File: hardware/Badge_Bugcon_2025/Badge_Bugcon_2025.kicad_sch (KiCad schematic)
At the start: 0 parts

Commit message: feat(Hw):Update_Schematic
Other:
- sheet MCU ports: added SCL, SDA; removed none
- sheet OLED ports: added DOWN, LEFT, RIGHT, SCL, SDA, UP, v_3v3; removed none

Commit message: feat(Hw):Update_Schematic
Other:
- sheet MCU ports: added DOWN, LEFT, RIGHT, UP; removed none
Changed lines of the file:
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@@
+	(wire
+		(pts
+			(xy 88.9 114.3) (xy 125.73 114.3)
+		)
+		(stroke
+			(width 0)
+			(type default)
+		)
+	)
 	(wire
 		(pts
@@
 	(wire
 		(pts
+			(xy 88.9 116.84) (xy 125.73 116.84)
+		)
+		(stroke
+			(width 0)
+			(type default)
+		)
+	)
+	(wire
+		(pts
 			(xy 181.61 113.03) (xy 181.61 147.32)
 		)
@@
 	(wire
 		(pts
+			(xy 88.9 111.76) (xy 125.73 111.76)
+		)
+		(stroke
+			(width 0)
+			(type default)
+		)
+	)
+	(wire
+		(pts
 			(xy 62.992 69.85) (xy 62.992 85.09)
 		)
@@
 		(pts
 			(xy 70.612 69.85) (xy 62.992 69.85)
+		)
+		(stroke
+			(width 0)
+			(type default)
+		)
+	)
+	(wire
+		(pts
+			(xy 88.9 109.22) (xy 125.73 109.22)
 		)
 		(stroke
@@
 			(effects
 				(font
+					(size 1.27 1.27)
+				)
+				(justify left)
+			)
+		)
+		(pin "DOWN" bidirectional
+			(at 125.73 114.3 180)
+			(effects
+				(font
+					(size 1.27 1.27)
+				)
+				(justify left)
+			)
+		)
+		(pin "LEFT" bidirectional
+			(at 125.73 111.76 180)
+			(effects
+				(font
+					(size 1.27 1.27)
+				)
+				(justify left)
+			)
+		)
+		(pin "RIGHT" bidirectional
+			(at 125.73 109.22 180)
+			(effects
+				(font
+					(size 1.27 1.27)
+				)
+				(justify left)
+			)
+		)
+		(pin "UP" bidirectional
+			(at 125.73 116.84 180)
+			(effects
+				(font

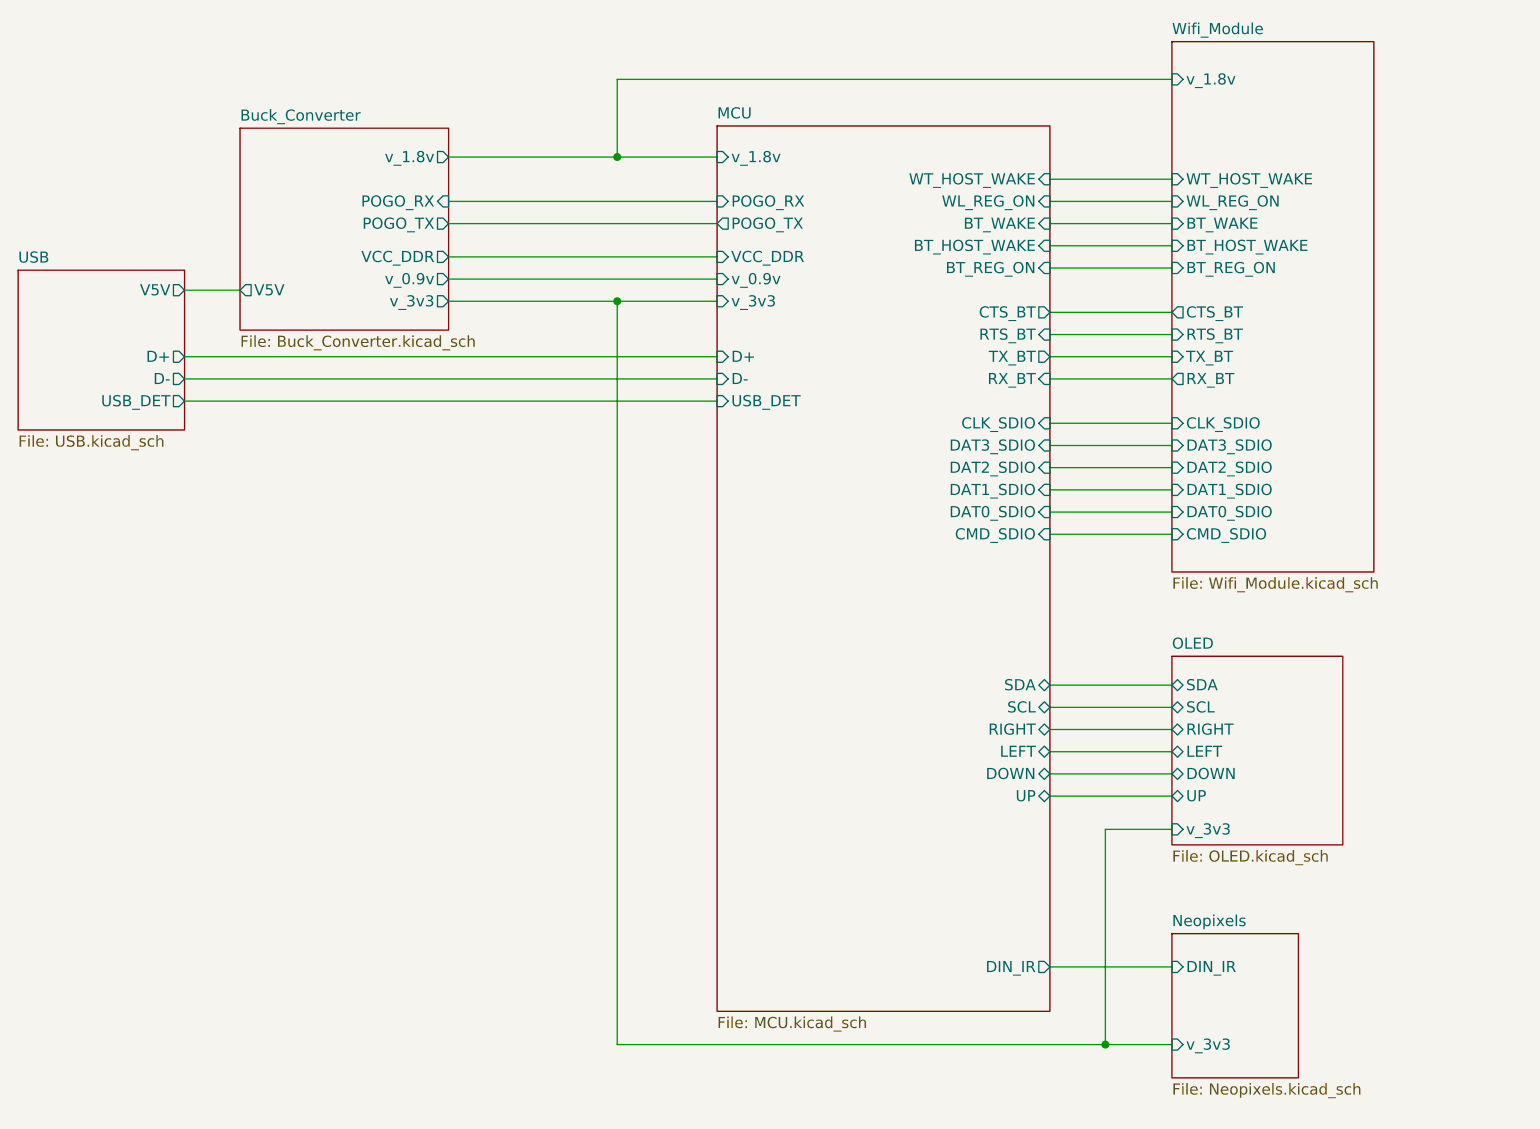
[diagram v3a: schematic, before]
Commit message: feat(Hw):Wifi_Module_Deleted
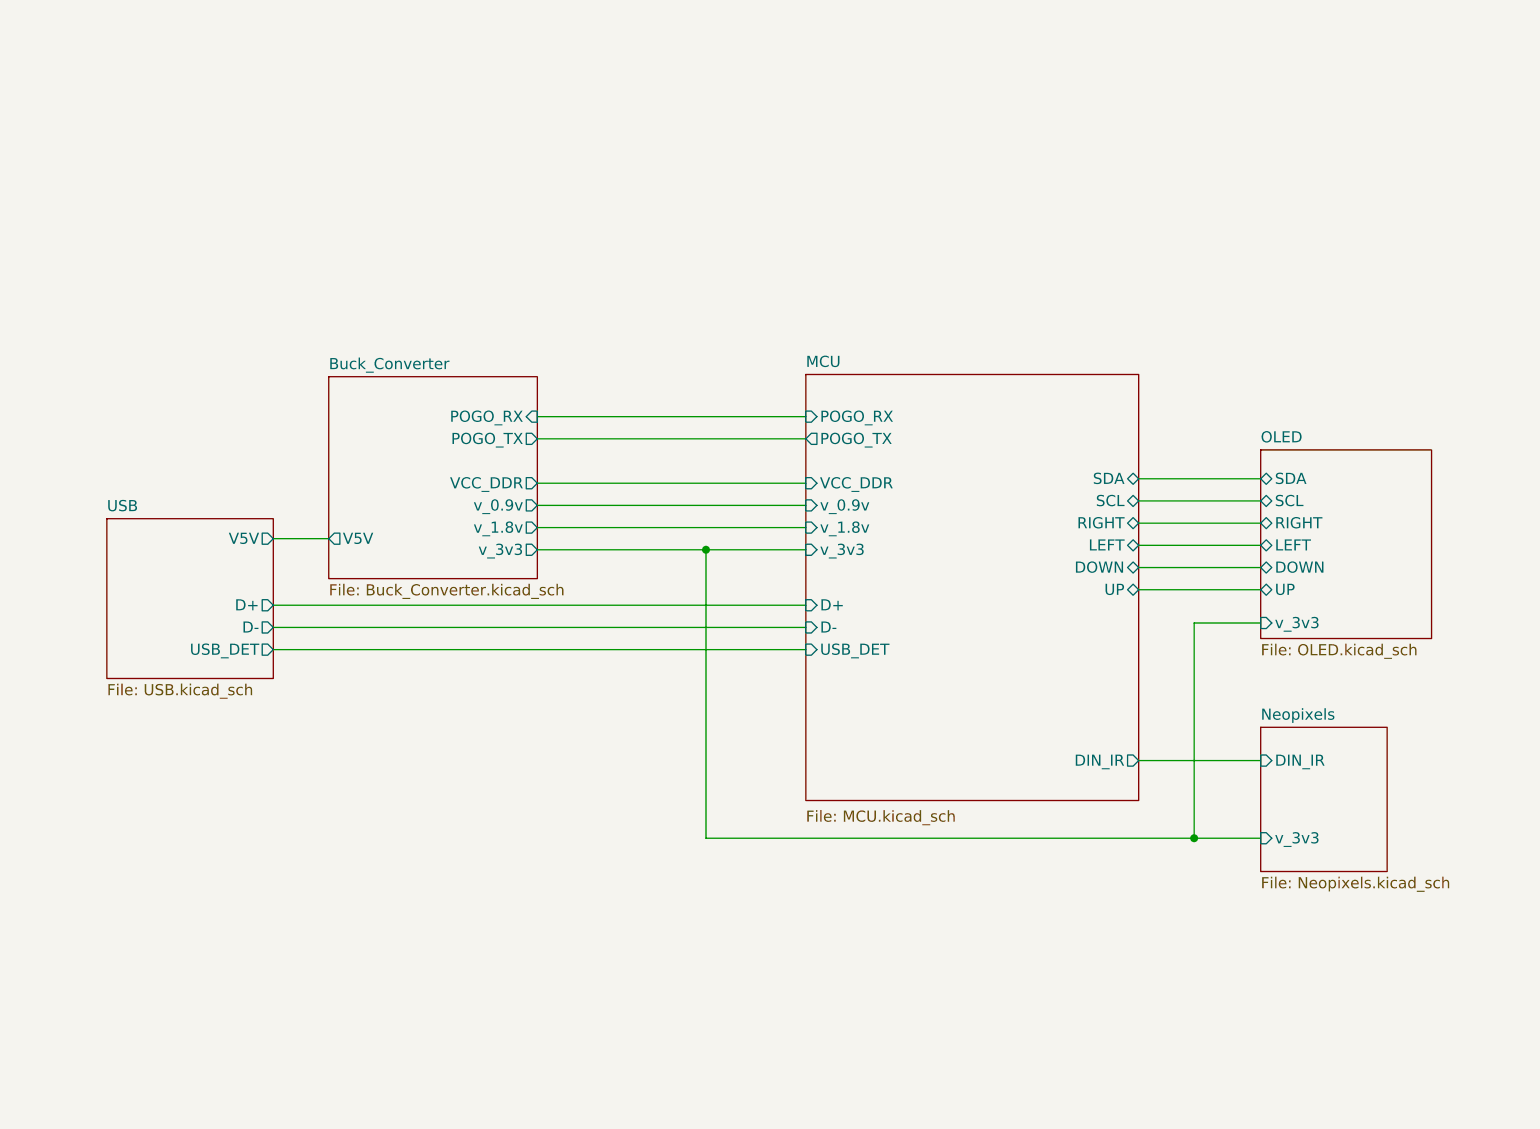
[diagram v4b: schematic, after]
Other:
- removed sheet Wifi_Module
- sheet MCU ports: added none; removed BT_HOST_WAKE, BT_REG_ON, BT_WAKE, CLK_SDIO, CMD_SDIO, CTS_BT, DAT0_SDIO, DAT1_SDIO, DAT2_SDIO, DAT3_SDIO, RTS_BT, RX_BT, TX_BT, WL_REG_ON, WT_HOST_WAKE

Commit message: feat(Hw):Update_Schematic
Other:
- sheet OLED renamed Add-On
- sheet Add-On ports: added none; removed DOWN, LEFT, RIGHT, UP
- sheet MCU ports: added none; removed DOWN, LEFT, RIGHT, UP
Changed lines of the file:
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@@
 	(paper "A4")
 	(junction
-		(at 185.42 116.078)
+		(at 179.07 104.14)
 		(diameter 0)
 		(color 255 23 32 1)
@@
 	(wire
 		(pts
-			(xy 129.54 83.058) (xy 129.54 116.078)
+			(xy 129.54 83.058) (xy 129.54 104.14)
 		)
 		(stroke
@@
 	(wire
 		(pts
-			(xy 179.07 77.47) (xy 193.04 77.47)
+			(xy 172.72 72.39) (xy 186.69 72.39)
 		)
 		(stroke
@@
 	(wire
 		(pts
-			(xy 179.07 82.55) (xy 193.04 82.55)
-		)
-		(stroke
-			(width 0)
-			(type default)
-		)
-	)
-	(wire
-		(pts
-			(xy 185.42 91.44) (xy 185.42 116.078)
+			(xy 179.07 78.74) (xy 179.07 104.14)
 		)
 		(stroke
@@
 	(wire
 		(pts
-			(xy 185.42 91.44) (xy 193.04 91.44)
+			(xy 179.07 78.74) (xy 186.69 78.74)
 		)
 		(stroke
@@
 	(wire
 		(pts
-			(xy 179.07 107.188) (xy 193.04 107.188)
+			(xy 172.72 93.98) (xy 186.69 93.98)
 		)
 		(stroke
@@
 	(wire
 		(pts
-			(xy 179.07 80.01) (xy 193.04 80.01)
-		)
-		(stroke
-			(width 0)
-			(type default)
-		)
-	)
-	(wire
-		(pts
-			(xy 179.07 85.09) (xy 193.04 85.09)
-		)
-		(stroke
-			(width 0)
-			(type default)
-		)
-	)
-	(wire
-		(pts
-			(xy 179.07 87.63) (xy 193.04 87.63)
-		)
-		(stroke
-			(width 0)
-			(type default)
-		)
-	)
-	(wire
-		(pts
 			(xy 80.01 89.408) (xy 140.97 89.408)
 		)
@@
 	(wire
 		(pts
-			(xy 185.42 116.078) (xy 193.04 116.078)
+			(xy 179.07 104.14) (xy 186.69 104.14)
 		)
 		(stroke
@@
 	(wire
 		(pts
-			(xy 179.07 74.93) (xy 193.04 74.93)
-		)
-		(stroke
-			(width 0)
-			(type default)
-		)
-	)
-	(wire
-		(pts
-			(xy 129.54 116.078) (xy 185.42 116.078)
+			(xy 172.72 69.85) (xy 186.69 69.85)
+		)
+		(stroke
+			(width 0)
+			(type default)
+		)
+	)
+	(wire
+		(pts
+			(xy 129.54 104.14) (xy 179.07 104.14)
 		)
 		(stroke
@@
 	)
 	(sheet
-		(at 193.04 71.628)
-		(size 19.558 21.59)
+		(at 186.69 65.024)
+		(size 19.558 16.764)
 		(exclude_from_sim no)
 		(in_bom yes)
@@
 			(color 0 0 0 0.0000)
 		)
-		(property "Sheetname" "OLED"
-			(at 193.04 70.9164 0)
+		(property "Sheetname" "Add-On"
+			(at 186.69 64.3124 0)
 			(effects
 				(font
@@
 		)
 		(property "Sheetfile" "OLED.kicad_sch"
-			(at 193.04 93.8026 0)
+			(at 186.69 82.3726 0)
 			(effects
 				(font
@@
 			)
 		)
-		(pin "DOWN" bidirectional
-			(at 193.04 85.09 180)
-			(effects
-				(font
-					(size 1.27 1.27)
-				)
-				(justify left)
-			)
-		)
-		(pin "LEFT" bidirectional
-			(at 193.04 82.55 180)
-			(effects
-				(font
-					(size 1.27 1.27)
-				)
-				(justify left)
-			)
-		)
-		(pin "RIGHT" bidirectional
-			(at 193.04 80.01 180)
-			(effects
-				(font
-					(size 1.27 1.27)
-				)
-				(justify left)
-			)
-		)
 		(pin "SCL" bidirectional
-			(at 193.04 77.47 180)
+			(at 186.69 72.39 180)
 			(effects
 				(font
@@
 		)
 		(pin "SDA" bidirectional
-			(at 193.04 74.93 180)
-			(effects
-				(font
-					(size 1.27 1.27)
-				)
-				(justify left)
-			)
-		)
-		(pin "UP" bidirectional
-			(at 193.04 87.63 180)
+			(at 186.69 69.85 180)
 			(effects
 				(font
@@
 		)
 		(pin "v_3v3" input
-			(at 193.04 91.44 180)
+			(at 186.69 78.74 180)
 			(effects
 				(font
@@
 	)
 	(sheet
-		(at 193.04 103.378)
-		(size 14.478 16.51)
+		(at 186.69 90.17)
+		(size 14.478 17.78)
 		(exclude_from_sim no)
 		(in_bom yes)
@@
 		)
 		(property "Sheetname" "Neopixels"
-			(at 193.04 102.6664 0)
+			(at 186.69 89.4584 0)
 			(effects
 				(font
@@
 		)
 		(property "Sheetfile" "Neopixels.kicad_sch"
-			(at 193.04 120.4726 0)
+			(at 186.69 108.5346 0)
 			(effects
 				(font
@@
 		)
 		(pin "DIN_IR" input
-			(at 193.04 107.188 180)
+			(at 186.69 93.98 180)
 			(effects
 				(font
@@
 		)
 		(pin "v_3v3" input
-			(at 193.04 116.078 180)
+			(at 186.69 104.14 180)
 			(effects
 				(font
@@
 	(sheet
 		(at 140.97 62.992)
-		(size 38.1 48.768)
+		(size 31.75 36.83)
 		(exclude_from_sim no)
 		(in_bom yes)
@@
 		)
 		(property "Sheetfile" "MCU.kicad_sch"
-			(at 140.97 112.8526 0)
+			(at 140.97 100.33 0)
 			(effects
 				(font
@@
 		)
 		(pin "DIN_IR" output
-			(at 179.07 107.188 0)
-			(effects
-				(font
-					(size 1.27 1.27)
-				)
-				(justify right)
-			)
-		)
-		(pin "DOWN" bidirectional
-			(at 179.07 85.09 0)
-			(effects
-				(font
-					(size 1.27 1.27)
-				)
-				(justify right)
-			)
-		)
-		(pin "LEFT" bidirectional
-			(at 179.07 82.55 0)
-			(effects
-				(font
-					(size 1.27 1.27)
-				)
-				(justify right)
-			)
-		)
-		(pin "RIGHT" bidirectional
-			(at 179.07 80.01 0)
+			(at 172.72 93.98 0)
 			(effects
 				(font
@@
 		)
 		(pin "SCL" bidirectional
-			(at 179.07 77.47 0)
+			(at 172.72 72.39 0)
 			(effects
 				(font
@@
 		)
 		(pin "SDA" bidirectional
-			(at 179.07 74.93 0)
-			(effects
-				(font
-					(size 1.27 1.27)
-				)
-				(justify right)
-			)
-		)
-		(pin "UP" bidirectional
-			(at 179.07 87.63 0)
-			(effects
-				(font
+			(at 172.72 69.85 0)
+			(effects
+				(font

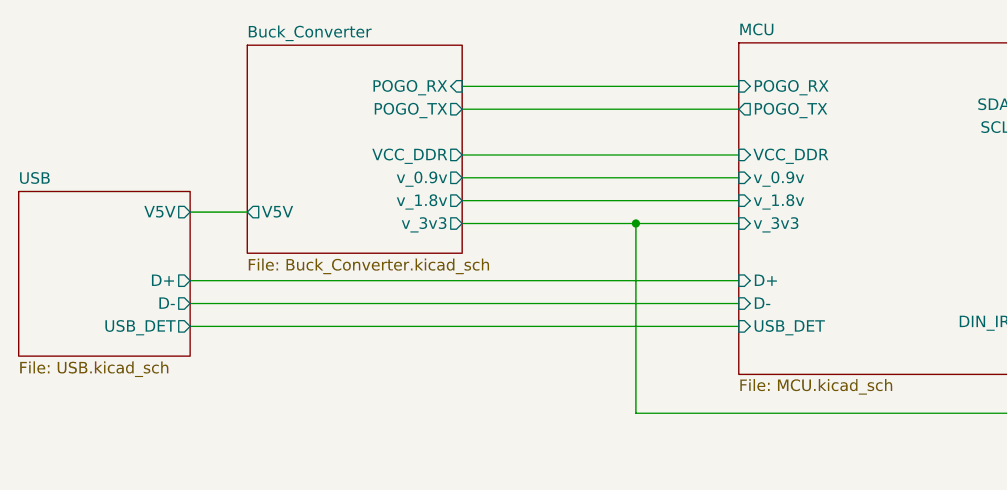
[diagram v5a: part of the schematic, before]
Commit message: feat(Hw):Update_Schematic_And_Floorplan
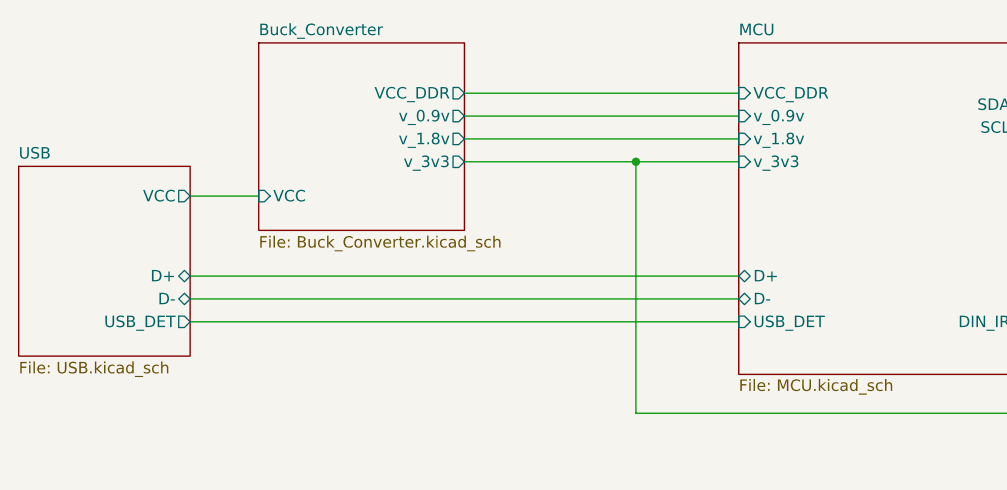
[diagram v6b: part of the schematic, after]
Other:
- sheet Buck_Converter ports: added VCC; removed POGO_RX, POGO_TX, V5V
- sheet MCU ports: added none; removed POGO_RX, POGO_TX
- sheet USB ports: added VCC; removed V5V
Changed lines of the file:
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@@
 	)
 	(junction
-		(at 129.54 83.058)
+		(at 129.54 76.2)
 		(diameter 0)
 		(color 255 23 32 1)
@@
 	(wire
 		(pts
-			(xy 110.236 83.058) (xy 129.54 83.058)
-		)
-		(stroke
-			(width 0)
-			(type default)
-			(color 255 23 32 1)
-		)
-	)
-	(wire
-		(pts
-			(xy 129.54 83.058) (xy 129.54 104.14)
+			(xy 80.01 80.01) (xy 87.63 80.01)
+		)
+		(stroke
+			(width 0)
+			(type default)
+		)
+	)
+	(wire
+		(pts
+			(xy 110.49 76.2) (xy 129.54 76.2)
+		)
+		(stroke
+			(width 0)
+			(type default)
+			(color 255 23 32 1)
+		)
+	)
+	(wire
+		(pts
+			(xy 129.54 76.2) (xy 129.54 104.14)
 		)
 		(stroke
@@
 	(wire
 		(pts
-			(xy 80.01 94.488) (xy 140.97 94.488)
-		)
-		(stroke
-			(width 0)
-			(type default)
-		)
-	)
-	(wire
-		(pts
-			(xy 110.236 80.518) (xy 140.97 80.518)
+			(xy 80.01 93.98) (xy 140.97 93.98)
+		)
+		(stroke
+			(width 0)
+			(type default)
+		)
+	)
+	(wire
+		(pts
+			(xy 110.49 73.66) (xy 140.97 73.66)
 		)
 		(stroke
@@
 	(wire
 		(pts
-			(xy 80.01 81.788) (xy 86.36 81.788)
-		)
-		(stroke
-			(width 0)
-			(type default)
-		)
-	)
-	(wire
-		(pts
 			(xy 172.72 93.98) (xy 186.69 93.98)
 		)
@@
 	(wire
 		(pts
-			(xy 110.236 77.978) (xy 140.97 77.978)
-		)
-		(stroke
-			(width 0)
-			(type default)
-		)
-	)
-	(wire
-		(pts
-			(xy 80.01 91.948) (xy 140.97 91.948)
-		)
-		(stroke
-			(width 0)
-			(type default)
-		)
-	)
-	(wire
-		(pts
-			(xy 129.54 83.058) (xy 140.97 83.058)
-		)
-		(stroke
-			(width 0)
-			(type default)
-			(color 255 23 32 1)
-		)
-	)
-	(wire
-		(pts
-			(xy 80.01 89.408) (xy 140.97 89.408)
-		)
-		(stroke
-			(width 0)
-			(type default)
+			(xy 110.49 71.12) (xy 140.97 71.12)
+		)
+		(stroke
+			(width 0)
+			(type default)
+		)
+	)
+	(wire
+		(pts
+			(xy 129.54 76.2) (xy 140.97 76.2)
+		)
+		(stroke
+			(width 0)
+			(type default)
+			(color 255 23 32 1)
 		)
 	)
@@
 	(wire
 		(pts
-			(xy 110.236 75.438) (xy 140.97 75.438)
+			(xy 110.49 68.58) (xy 140.97 68.58)
 		)
 		(stroke
@@
 	(wire
 		(pts
-			(xy 110.236 70.358) (xy 140.97 70.358)
-		)
-		(stroke
-			(width 0)
-			(type default)
-		)
-	)
-	(wire
-		(pts
-			(xy 110.236 67.818) (xy 140.97 67.818)
+			(xy 80.01 91.44) (xy 140.97 91.44)
+		)
+		(stroke
+			(width 0)
+			(type default)
+		)
+	)
+	(wire
+		(pts
+			(xy 80.01 88.9) (xy 140.97 88.9)
 		)
 		(stroke
@@
 	)
 	(sheet
-		(at 86.36 63.246)
-		(size 23.876 23.114)
+		(at 87.63 62.992)
+		(size 22.86 20.828)
 		(exclude_from_sim no)
 		(in_bom yes)
@@
 		)
 		(property "Sheetname" "Buck_Converter"
-			(at 86.36 62.5344 0)
+			(at 87.63 62.2804 0)
 			(effects
 				(font
@@
 		)
 		(property "Sheetfile" "Buck_Converter.kicad_sch"
-			(at 86.36 86.9446 0)
+			(at 87.63 84.4046 0)
 			(effects
 				(font
@@
 			)
 		)
-		(pin "POGO_RX" input
-			(at 110.236 67.818 0)
-			(effects
-				(font
-					(size 1.27 1.27)
-				)
-				(justify right)
-			)
-		)
-		(pin "POGO_TX" output
-			(at 110.236 70.358 0)
-			(effects
-				(font
-					(size 1.27 1.27)
-				)
-				(justify right)
-			)
-		)
-		(pin "V5V" output
-			(at 86.36 81.788 180)
-			(effects
-				(font
-					(size 1.27 1.27)
-				)
-				(justify left)
-			)
-		)
 		(pin "VCC_DDR" output
-			(at 110.236 75.438 0)
+			(at 110.49 68.58 0)
 			(effects
 				(font
@@
 		)
 		(pin "v_0.9v" output
-			(at 110.236 77.978 0)
+			(at 110.49 71.12 0)
 			(effects
 				(font
@@
 		)
 		(pin "v_1.8v" output
-			(at 110.236 80.518 0)
+			(at 110.49 73.66 0)
 			(effects
 				(font
@@
 		)
 		(pin "v_3v3" output
-			(at 110.236 83.058 0)
-			(effects
-				(font
-					(size 1.27 1.27)
-				)
-				(justify right)
+			(at 110.49 76.2 0)
+			(effects
+				(font
+					(size 1.27 1.27)
+				)
+				(justify right)
+			)
+		)
+		(pin "VCC" input
+			(at 87.63 80.01 180)
+			(effects
+				(font
+					(size 1.27 1.27)
+				)
+				(justify left)
 			)
 		)
@@
 	)
 	(sheet
-		(at 60.96 79.502)
-		(size 19.05 18.288)
+		(at 60.96 76.708)
+		(size 19.05 21.082)
 		(exclude_from_sim no)
 		(in_bom yes)
@@
 		)
 		(property "Sheetname" "USB"
-			(at 60.96 78.7904 0)
+			(at 60.96 75.9964 0)
 			(effects
 				(font
@@
 			)
 		)
-		(pin "D+" output
-			(at 80.01 89.408 0)
-			(effects
-				(font
-					(size 1.27 1.27)
-				)
-				(justify right)
-			)
-		)
-		(pin "D-" output
-			(at 80.01 91.948 0)
-			(effects
-				(font
-					(size 1.27 1.27)
-				)
-				(justify right)
-			)
-		)
 		(pin "USB_DET" output
-			(at 80.01 94.488 0)
-			(effects
-				(font
-					(size 1.27 1.27)
-				)
-				(justify right)
-			)
-		)
-		(pin "V5V" output
-			(at 80.01 81.788 0)
+			(at 80.01 93.98 0)
+			(effects
+				(font
+					(size 1.27 1.27)
+				)
+				(justify right)
+			)
+		)
+		(pin "VCC" output
+			(at 80.01 80.01 0)
+			(effects
+				(font
+					(size 1.27 1.27)
+				)
+				(justify right)
+			)
+		)
+		(pin "D+" bidirectional
+			(at 80.01 88.9 0)
+			(effects
+				(font
+					(size 1.27 1.27)
+				)
+				(justify right)
+			)
+		)
+		(pin "D-" bidirectional
+			(at 80.01 91.44 0)
 			(effects
 				(font
@@
 			)
 		)
-		(pin "POGO_RX" input
-			(at 140.97 67.818 180)
-			(effects
-				(font
-					(size 1.27 1.27)
-				)
-				(justify left)
-			)
-		)
-		(pin "POGO_TX" output
-			(at 140.97 70.358 180)
-			(effects
-				(font
-					(size 1.27 1.27)
-				)
-				(justify left)
-			)
-		)
 		(pin "VCC_DDR" input
-			(at 140.97 75.438 180)
+			(at 140.97 68.58 180)
 			(effects
 				(font
@@
 		)
 		(pin "v_0.9v" input
-			(at 140.97 77.978 180)
+			(at 140.97 71.12 180)
 			(effects
 				(font
@@
 		)
 		(pin "v_1.8v" input
-			(at 140.97 80.518 180)
+			(at 140.97 73.66 180)
 			(effects
 				(font
@@
 		)
 		(pin "v_3v3" input
-			(at 140.97 83.058 180)
-			(effects
-				(font
-					(size 1.27 1.27)
-				)
-				(justify left)
-			)
-		)
-		(pin "D+" input
-			(at 140.97 89.408 180)
-			(effects
-				(font
-					(size 1.27 1.27)
-				)
-				(justify left)
-			)
-		)
-		(pin "D-" input
-			(at 140.97 91.948 180)
+			(at 140.97 76.2 180)
 			(effects
 				(font
@@
 		)
 		(pin "USB_DET" input
-			(at 140.97 94.488 180)
+			(at 140.97 93.98 180)
 			(effects
 				(font
@@
 			)
 		)
+		(pin "D+" bidirectional
+			(at 140.97 88.9 180)
+			(effects
+				(font
+					(size 1.27 1.27)
+				)
+				(justify left)
+			)
+		)
+		(pin "D-" bidirectional
+			(at 140.97 91.44 180)
+			(effects
+				(font
+					(size 1.27 1.27)
+				)
+				(justify left)
+			)
+		)
